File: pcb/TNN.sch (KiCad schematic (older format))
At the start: 6 parts, among them P1 CONN_01X10, P2 CONN_01X04, P3 CONN_01X10, P4 CONN_01X04, SW1 SPST

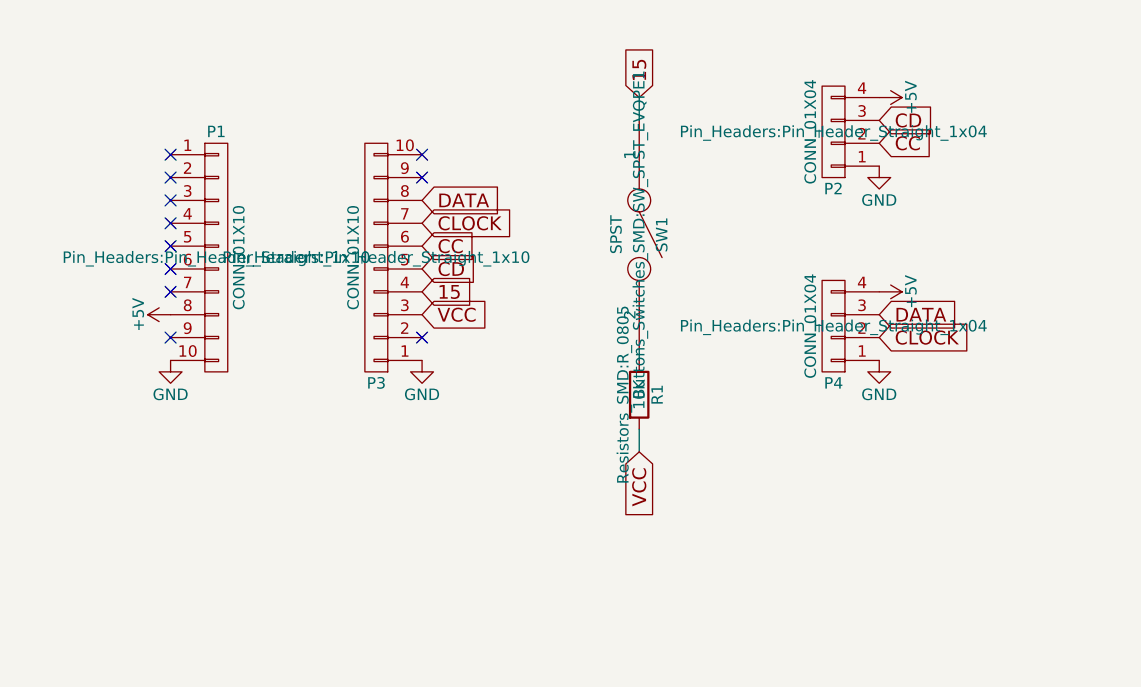
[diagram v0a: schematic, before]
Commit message: [*] move left (1x10 head pins) 7*.05 inches.
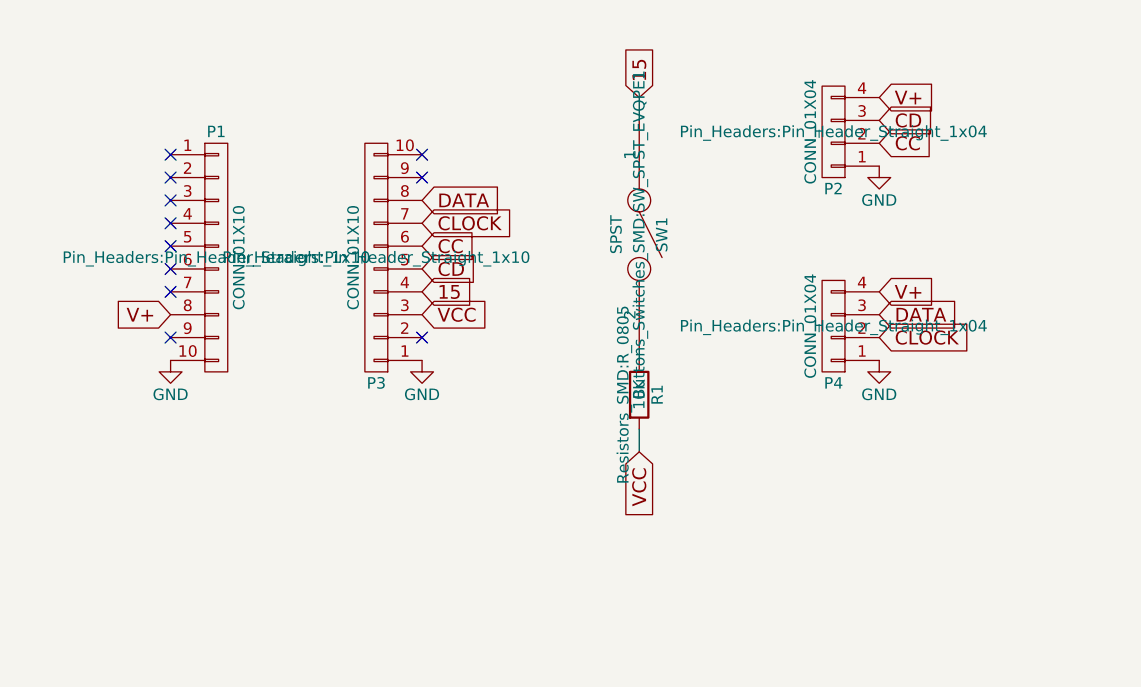
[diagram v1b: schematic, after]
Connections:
- net +5V renamed V+
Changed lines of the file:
@@
 	1    0    0    -1
-$EndComp
-$Comp
-L +5V #PWR03
-U 1 1 5808FE65
-P 1150 1700
-F 0 "#PWR03" H 1150 1550 50  0001 C CNN
-F 1 "+5V" H 1150 1840 50  0000 C CNN
-F 2 "" H 1150 1700 50  0000 C CNN
-F 3 "" H 1150 1700 50  0000 C CNN
-	1    1150 1700
-	0    -1   -1   0
 $EndComp
 Text GLabel 2250 1600 2    60   Input ~ 0
@@
 	1    4050 1750
 	-1   0    0    1
-$EndComp
-$Comp
-L +5V #PWR04
-U 1 1 5809075C
-P 4250 1600
-F 0 "#PWR04" H 4250 1450 50  0001 C CNN
-F 1 "+5V" H 4250 1740 50  0000 C CNN
-F 2 "" H 4250 1600 50  0000 C CNN
-F 3 "" H 4250 1600 50  0000 C CNN
-	1    4250 1600
-	0    1    1    0
 $EndComp
 $Comp
@@
 Text GLabel 4250 850  2    60   Input ~ 0
 CD
-$Comp
-L +5V #PWR06
-U 1 1 58090AFE
-P 4250 750
-F 0 "#PWR06" H 4250 600 50  0001 C CNN
-F 1 "+5V" H 4250 890 50  0000 C CNN
-F 2 "" H 4250 750 50  0000 C CNN
-F 3 "" H 4250 750 50  0000 C CNN
-	1    4250 750
-	0    1    1    0
-$EndComp
 $Comp
 L GND #PWR07
@@
 Wire Wire Line
 	3200 2200 3200 2300
+Text GLabel 4250 1600 2    60   Input ~ 0
+V+
+Text GLabel 4250 750  2    60   Input ~ 0
+V+
+Text GLabel 1150 1700 0    60   Input ~ 0
+V+
 $EndSCHEMATC

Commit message: [*] Flip over.
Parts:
- removed P2: CONN_01X04, Pin_Headers:Pin_Header_Straight_1x04, symbol CONN_01X04
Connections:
- net 15: now also R1.1
- net GND: now also R1.2
- net VCC: now also SW1.2; no longer R1.2
- net CC: no longer names the net of P3.6 (P6)
- net CD: no longer names the net of P3.5 (P5)
- net CLOCK renamed 4-CLOCK
- net DATA renamed 5-DATA
- no-connect marks 11 -> 13
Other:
- moved on the sheet: P4, R1, SW1
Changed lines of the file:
@@
 $EndComp
 Text GLabel 2250 1300 2    60   Input ~ 0
-CLOCK
+4-CLOCK
 Text GLabel 2250 1200 2    60   Input ~ 0
-DATA
+5-DATA
 $Comp
 L R R1
 U 1 1 5808FF31
-P 3200 2050
-F 0 "R1" V 3280 2050 50  0000 C CNN
-F 1 "10K" V 3200 2050 50  0000 C CNN
-F 2 "Resistors_SMD:R_0805" V 3130 2050 50  0000 C CNN
-F 3 "" H 3200 2050 50  0000 C CNN
-	1    3200 2050
+P 3200 2750
+F 0 "R1" V 3280 2750 50  0000 C CNN
+F 1 "10K" V 3200 2750 50  0000 C CNN
+F 2 "Resistors_SMD:R_0805" V 3130 2750 50  0000 C CNN
+F 3 "" H 3200 2750 50  0000 C CNN
+	1    3200 2750
 	1    0    0    -1
 $EndComp
 Text GLabel 2250 1700 2    60   Input ~ 0
 VCC
-Text GLabel 3200 750  1    60   Input ~ 0
+Text GLabel 3650 1850 2    60   Input ~ 0
 15
 $Comp
 L GND #PWR01
-U 1 1 5808FBE5
-P 2250 1900
-F 0 "#PWR01" H 2250 1650 50  0001 C CNN
-F 1 "GND" H 2250 1750 50  0000 C CNN
-F 2 "" H 2250 1900 50  0000 C CNN
-F 3 "" H 2250 1900 50  0000 C CNN
-	1    2250 1900
-	1    0    0    -1
-$EndComp
-$Comp
-L GND #PWR02
 U 1 1 5808FC4B
 P 1150 1900
-F 0 "#PWR02" H 1150 1650 50  0001 C CNN
+F 0 "#PWR01" H 1150 1650 50  0001 C CNN
 F 1 "GND" H 1150 1750 50  0000 C CNN
 F 2 "" H 1150 1900 50  0000 C CNN
@@
 Text GLabel 2250 1600 2    60   Input ~ 0
 15
-Text GLabel 3200 2300 3    60   Input ~ 0
+Text GLabel 3200 750  1    60   Input ~ 0
 VCC
 $Comp
 L CONN_01X04 P4
 U 1 1 580905C2
-P 4050 1750
-F 0 "P4" H 4050 2000 50  0000 C CNN
-F 1 "CONN_01X04" V 4150 1750 50  0000 C CNN
-F 2 "Pin_Headers:Pin_Header_Straight_1x04" H 4050 1750 50  0000 C CNN
-F 3 "" H 4050 1750 50  0000 C CNN
-	1    4050 1750
+P 4450 1000
+F 0 "P4" H 4450 1250 50  0000 C CNN
+F 1 "CONN_01X04" V 4550 1000 50  0000 C CNN
+F 2 "Pin_Headers:Pin_Header_Straight_1x04" H 4450 1000 50  0000 C CNN
+F 3 "" H 4450 1000 50  0000 C CNN
+	1    4450 1000
 	-1   0    0    1
 $EndComp
 $Comp
-L GND #PWR05
+L GND #PWR02
 U 1 1 58090796
-P 4250 1900
-F 0 "#PWR05" H 4250 1650 50  0001 C CNN
-F 1 "GND" H 4250 1750 50  0000 C CNN
-F 2 "" H 4250 1900 50  0000 C CNN
-F 3 "" H 4250 1900 50  0000 C CNN
-	1    4250 1900
+P 4650 1150
+F 0 "#PWR02" H 4650 900 50  0001 C CNN
+F 1 "GND" H 4650 1000 50  0000 C CNN
+F 2 "" H 4650 1150 50  0000 C CNN
+F 3 "" H 4650 1150 50  0000 C CNN
+	1    4650 1150
 	1    0    0    -1
 $EndComp
-Text GLabel 4250 1700 2    60   Input ~ 0
-DATA
-Text GLabel 4250 1800 2    60   Input ~ 0
-CLOCK
-$Comp
-L CONN_01X04 P2
-U 1 1 580908DE
-P 4050 900
-F 0 "P2" H 4050 1150 50  0000 C CNN
-F 1 "CONN_01X04" V 4150 900 50  0000 C CNN
-F 2 "Pin_Headers:Pin_Header_Straight_1x04" H 4050 900 50  0000 C CNN
-F 3 "" H 4050 900 50  0000 C CNN
-	1    4050 900
-	-1   0    0    1
-$EndComp
-Text GLabel 2250 1500 2    60   Input ~ 0
-CD
-Text GLabel 2250 1400 2    60   Input ~ 0
-CC
-Text GLabel 4250 950  2    60   Input ~ 0
-CC
-Text GLabel 4250 850  2    60   Input ~ 0
-CD
-$Comp
-L GND #PWR07
-U 1 1 58090B86
-P 4250 1050
-F 0 "#PWR07" H 4250 800 50  0001 C CNN
-F 1 "GND" H 4250 900 50  0000 C CNN
-F 2 "" H 4250 1050 50  0000 C CNN
-F 3 "" H 4250 1050 50  0000 C CNN
-	1    4250 1050
-	1    0    0    -1
-$EndComp
+Text GLabel 4650 950  2    60   Input ~ 0
+5-DATA
+Text GLabel 4650 1050 2    60   Input ~ 0
+4-CLOCK
 $Comp
 L SPST SW1
@@
 P 3200 1350
 F 0 "SW1" H 3200 1450 50  0000 C CNN
-F 1 "SPST" H 3200 1250 50  0000 C CNN
+F 1 "SPST" V 3200 1250 50  0000 C CNN
 F 2 "Buttons_Switches_SMD:SW_SPST_EVQPE1" H 3200 1350 50  0000 C CNN
 F 3 "" H 3200 1350 50  0000 C CNN
 	1    3200 1350
-	0    1    1    0
+	0    -1   -1   0
 $EndComp
-Wire Wire Line
-	3200 1900 3200 1850
 Wire Wire Line
 	3200 750  3200 850
@@
 NoConn ~ 2250 1800
 NoConn ~ 1150 1800
-NoConn ~ 1150 1600
-NoConn ~ 1150 1400
 NoConn ~ 1150 1300
 NoConn ~ 1150 1200
 NoConn ~ 1150 1100
 NoConn ~ 1150 1000
-NoConn ~ 1150 1500
 Wire Wire Line
-	3200 2200 3200 2300
-Text GLabel 4250 1600 2    60   Input ~ 0
-V+
-Text GLabel 4250 750  2    60   Input ~ 0
+	3200 2900 3200 3000
+Text GLabel 4650 850  2    60   Input ~ 0
 V+
 Text GLabel 1150 1700 0    60   Input ~ 0
 V+
+NoConn ~ 2250 1400
+NoConn ~ 2250 1500
+$Comp
+L GND #PWR03
+U 1 1 580A5F4D
+P 3200 3000
+F 0 "#PWR03" H 3200 2750 50  0001 C CNN
+F 1 "GND" H 3200 2850 50  0000 C CNN
+F 2 "" H 3200 3000 50  0000 C CNN
+F 3 "" H 3200 3000 50  0000 C CNN
+	1    3200 3000
+	1    0    0    -1
+$EndComp
+Connection ~ 3200 750
+NoConn ~ 1150 1500
+NoConn ~ 1150 1600
+NoConn ~ 1150 1400
+$Comp
+L GND #PWR04
+U 1 1 5808FBE5
+P 2250 1900
+F 0 "#PWR04" H 2250 1650 50  0001 C CNN
+F 1 "GND" H 2250 1750 50  0000 C CNN
+F 2 "" H 2250 1900 50  0000 C CNN
+F 3 "" H 2250 1900 50  0000 C CNN
+	1    2250 1900
+	1    0    0    -1
+$EndComp
+Wire Wire Line
+	3650 1850 3200 1850
+Wire Wire Line
+	3200 1850 3200 2600
 $EndSCHEMATC
